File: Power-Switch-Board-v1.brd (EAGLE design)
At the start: 23.5 x 8.3 mm, 7 parts, among them U3 CPH3356-TL-W

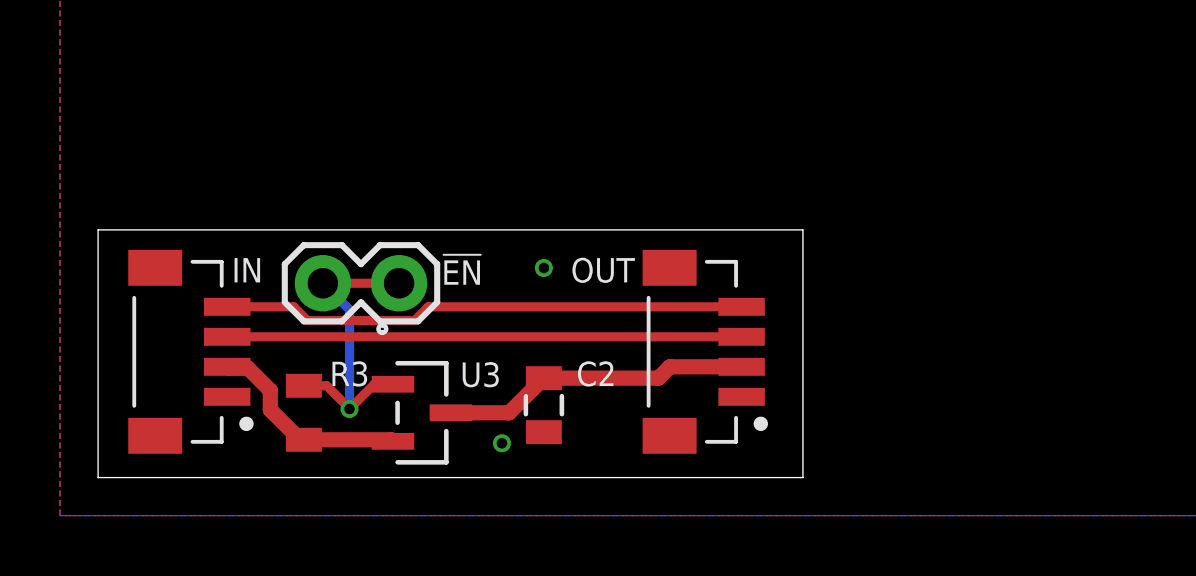
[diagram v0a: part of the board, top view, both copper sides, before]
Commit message: Updated for 0.1" headers
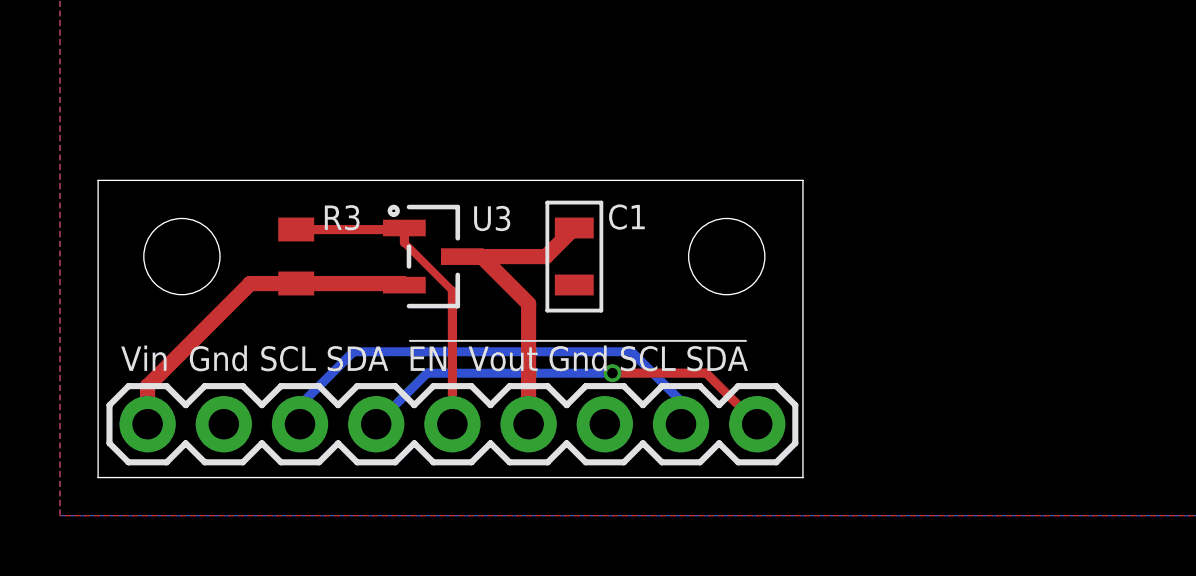
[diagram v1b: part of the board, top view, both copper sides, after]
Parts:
- removed !EN: (no value), SparkFun-Connectors:1X02
- removed C2: 0.1uF, Custom Components:0805@1
- removed IN, OUT: BM04B-SRSS-TBT(LF)(SN), Custom Components:CONN_BM04B-SRSS-TBT(LF)(SN)
- added C1: (no value), Custom Components:C0805
- added H1, H2: STAND-OFF-M2.5, Custom Components:STAND-OFF-M2.5
- added J1: (no value), SparkFun-Connectors:1X09
- moved U3 5.22 mm to (11.2, 7.37)
- moved R3 5.21 mm to (6.60, 7.37)
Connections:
- net !EN: now also J1.5; no longer !EN.1, !EN.2
- net GND: now also C1.P$2, J1.2, J1.7; no longer C2.2, IN.1, IN.SH1, IN.SH2, OUT.1, OUT.SH1, OUT.SH2
- net SCL: now also J1.3, J1.8; no longer IN.4, OUT.4
- net SDA: now also J1.4, J1.9; no longer IN.3, OUT.3
- net VCC-IN: now also J1.1; no longer IN.2
- net VCC-OUT: now also C1.P$1, J1.6; no longer C2.1, OUT.2
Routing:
- net VCC-IN: track 6.93 -> 11.3 mm
- net SDA: track 17.1 -> 14.1 mm, vias 0 -> 1
- net SCL: track 17.5 -> 15.5 mm
- net VCC-OUT: track 10.3 -> 11.0 mm
- net !EN: track 10.7 -> 10.8 mm, vias 1 -> 0
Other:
- board size 23.5 x 8.3 mm -> 23.5 x 9.9 mm
- board text added: "20V / 2.5A, 137mOhm, 1.8V logic"
- board text added: "Power Switch Board v1a 12-14-21"
- board text added: "Vin Gnd SCL SDA !EN Vout Gnd SCL SDA"
- board text removed: "-20, 137mOhm, -2.5A, 1.8V drive"
- board text removed: "Power Switch Board v1 12-10-21"
